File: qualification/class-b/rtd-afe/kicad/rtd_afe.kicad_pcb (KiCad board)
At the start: 4 copper layers, 72 x 56 mm, 54 parts, among them J1 TYPE-C-31-M-12, J2 PT100, J3 SWD, U1 ADS124S08IRHBR, U2 RP2350A, U3 REF5025AIDR, U4 W25Q128JVSIQ, U5 LDO, Y1 12MHz

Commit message: SYN-363 - compact the RTD board and add angled and schematic views
Signed-off-by: nyagamunene <stevenyaga2014@gmail.com>
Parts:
- moved H4 7.21 mm to (64.0, 49.0)
- moved J1 6.25 mm to (55.0, 5.24)
- moved C_L1 6.00 mm to (58.5, 20.0)
- moved C_L2 6.00 mm to (63.0, 21.5)
- moved D1 6.00 mm to (52.5, 16.0)
- moved D2 6.00 mm to (56.0, 16.0)
- moved H2 6.00 mm to (64.0, 4.00)
- moved R_CC1 6.00 mm to (59.0, 12.0)
- moved R_CC2 6.00 mm to (51.0, 12.0)
- moved U5 6.00 mm to (62.0, 17.0)
- moved C_IO1 5.01 mm to (42.0, 35.0)
- moved C_F 4.61 mm to (36.0, 48.0)
- moved J3 4.47 mm to (53.5, 48.0)
- moved H3 4.00 mm to (4.00, 49.0)
- moved J2 2.50 mm to (28.8, 50.0)
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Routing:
- net SWDIO: track 23.2 -> 13.7 mm
- net VBUS: track 27.2 -> 21.2 mm
- net ADC_RESET_N: track 25.9 -> 20.3 mm
- net AIN1: track 19.8 -> 25.1 mm
- net SWCLK: track 19.6 -> 14.9 mm
- net DGND: track 4.65 -> 0.00 mm, vias 26 -> 25
- net USB_DN_C: track 21.6 -> 17.1 mm
- net USB_DP_C: track 21.6 -> 17.1 mm
- net USB_DN: track 12.2 -> 8.85 mm, vias 2 -> 0
- net RTD_FP: track 25.2 -> 28.5 mm
- net USB_DP: track 8.28 -> 11.5 mm
- net RTD_SP: track 6.98 -> 4.48 mm
- net RTD_SN: track 6.79 -> 4.29 mm
- net +3V3: track 158.3 -> 160.5 mm
- net QSPI_SD1: track 16.7 -> 18.7 mm
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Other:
- board size 72 x 56 mm -> 66 x 53 mm

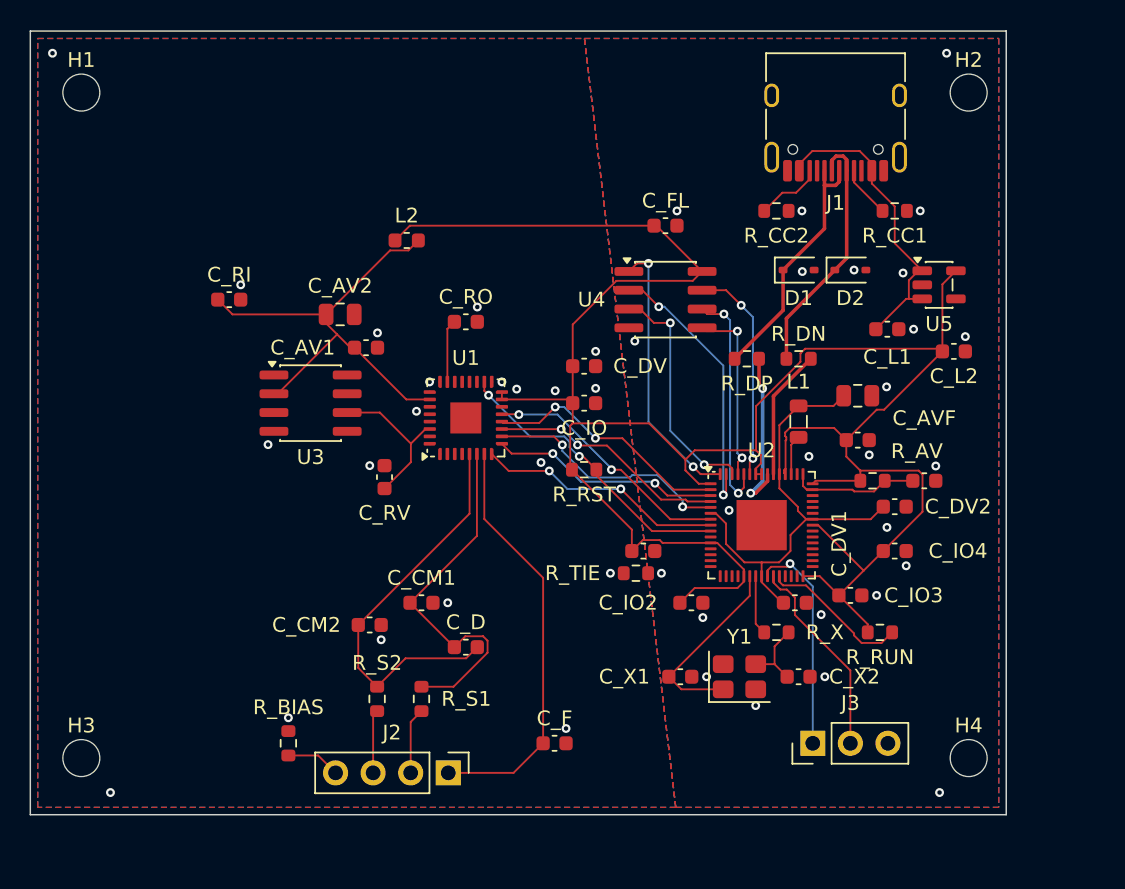
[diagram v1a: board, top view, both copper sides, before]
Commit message: SYN-363 - tighten the RTD board to 63 x 51 mm
Signed-off-by: nyagamunene <stevenyaga2014@gmail.com>
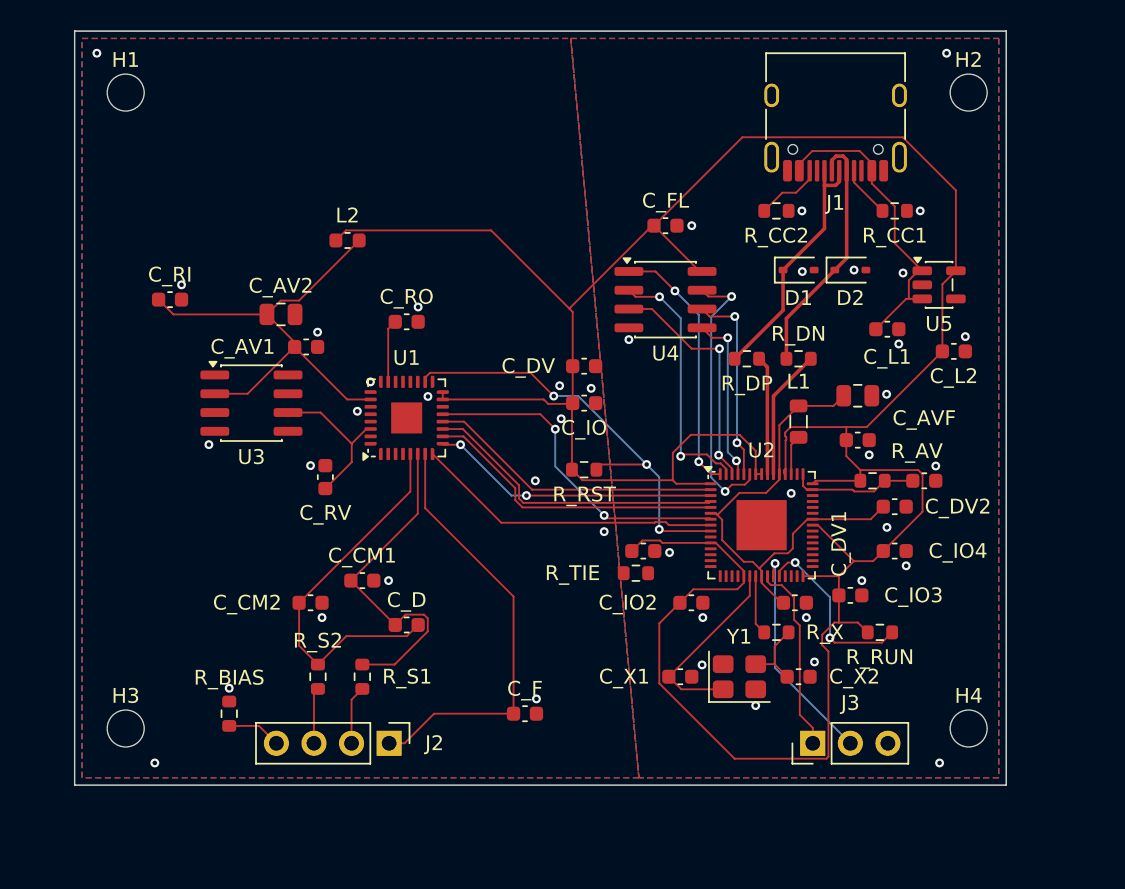
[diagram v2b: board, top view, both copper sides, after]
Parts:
- moved J2 4.47 mm to (24.8, 48.0)
- moved R_BIAS 4.47 mm to (14.0, 46.0)
- moved C_CM1 4.27 mm to (23.0, 37.0)
- moved C_CM2 4.27 mm to (19.5, 38.5)
- moved C_D 4.27 mm to (26.0, 40.0)
- moved R_S1 4.27 mm to (23.0, 43.5)
- moved R_S2 4.27 mm to (20.0, 43.5)
- moved C_AV1 4.05 mm to (19.2, 21.2)
- moved C_AV2 4.00 mm to (17.5, 19.0)
- moved C_RI 4.00 mm to (10.0, 18.0)
- moved C_RO 4.00 mm to (26.0, 19.5)
- moved C_RV 4.00 mm to (20.5, 30.0)
- moved L2 4.00 mm to (22.0, 14.0)
- moved U1 4.00 mm to (26.0, 26.0)
- moved U3 4.00 mm to (15.5, 25.0)
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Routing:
- net +3V3: track 160.5 -> 200.0 mm
- net ADC_RESET_N: track 20.3 -> 29.8 mm, vias 2 -> 3
- net ADC_DRDY: track 17.1 -> 22.5 mm
- net SPI_SCK: track 16.2 -> 20.7 mm, vias 2 -> 0
- net ADC_START: track 16.8 -> 20.8 mm, vias 2 -> 0
- net SPI_CS: track 15.6 -> 19.6 mm
- net SPI_MOSI: track 16.7 -> 20.6 mm, vias 2 -> 0
- net QSPI_SD3: track 14.9 -> 18.7 mm
- net USB_DP: track 11.5 -> 8.04 mm, vias 2 -> 0
- net SPI_MISO: track 16.9 -> 20.0 mm, vias 2 -> 0
- net RUN: track 10.1 -> 12.4 mm, vias 0 -> 2
- net QSPI_SCLK: track 15.6 -> 13.3 mm
- net SWCLK: track 14.9 -> 13.0 mm, vias 1 -> 0
- net DVDD_1V1: track 31.7 -> 33.5 mm
- net AIN1: track 25.1 -> 23.5 mm
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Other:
- board size 66 x 53 mm -> 63 x 51 mm

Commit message: SYN-363 - re-place and compact the RTD board to 50 x 44 mm
Rebuild the floorplan around the signal chain instead of scaling it: analog chain and input filter on the left, MCU/flash/crystal and USB on the right, connectors on the edges. The board drops from 63.1 x 51.1 mm to 50.1 x 44.1 mm.

- U2/U4 9.6 mm apart, Y1 below U2, USB-C at the top edge, SWD and PT100 at the bottom.
- R_TIE moved to the AGND/DGND bisector at (31.4, 31.5); all 54 ground pads sit on their own side of the split.
- 349 segments, 61 vias, 597.1 mm of copper, 41 nets connected, 0 open.
- KiCad DRC 0 errors / 0 warnings / 0 unconnected, ERC 0 errors / 2 library warnings, tie check R_TIE only.
- U1 label moved; 24 passive/TVS reference labels hidden where the compact layout has no clear spot (refdes remain in BOM, PnP, schematic).
- Record the all-absolute sidecar re-packing defect and refresh QUALIFICATION/SHA256SUMS.
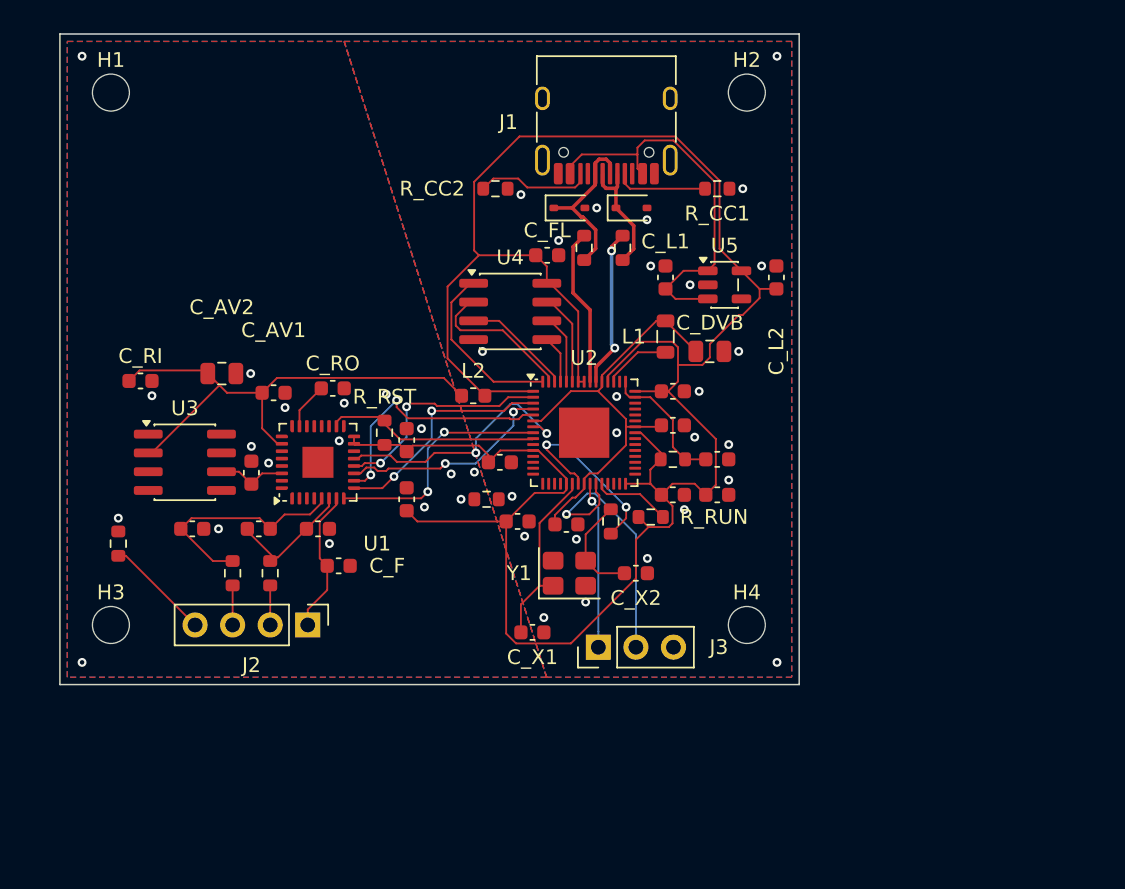
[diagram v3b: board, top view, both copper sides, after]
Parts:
- moved R_CC2 19.1 mm to (32.0, 10.5)
- moved R_RUN 17.4 mm to (42.5, 32.7)
- moved H4 16.6 mm to (49.0, 40.0)
- moved C_DV1 16.3 mm to (36.8, 33.2)
- moved C_F 16.1 mm to (21.4, 36.0)
- moved D1 16.1 mm to (37.0, 11.8)
- moved C_DV2 16.0 mm to (44.0, 26.5)
- moved J3 15.9 mm to (39.0, 41.5)
- moved J1 15.5 mm to (39.5, 5.44)
- moved C_L1 15.4 mm to (43.5, 16.5), turned to 90 degrees
- moved D2 15.4 mm to (41.2, 11.8)
- moved H2 15.0 mm to (49.0, 4.00)
- moved U5 14.5 mm to (47.5, 17.0)
- moved C_AVF 14.1 mm to (47.0, 28.8)
- moved R_DN 14.1 mm to (40.6, 14.5), turned to 90 degrees
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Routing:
- net +3V3: track 200.0 -> 159.7 mm
- net RTD_FP: track 29.3 -> 9.79 mm
- net ADC_RESET_N: track 29.8 -> 14.5 mm, vias 3 -> 0
- net AIN1: track 23.5 -> 8.72 mm
- net QSPI_SD3: track 18.7 -> 6.25 mm, vias 2 -> 0
- net AIN2: track 25.8 -> 15.6 mm
- net XOUT: track 4.04 -> 13.0 mm, vias 0 -> 2
- net QSPI_SD2: track 16.1 -> 7.40 mm, vias 2 -> 0
- net USB_DN_C: track 17.1 -> 8.45 mm
- net QSPI_SCLK: track 13.3 -> 4.80 mm, vias 2 -> 0
- net QSPI_SD0: track 11.5 -> 3.23 mm, vias 2 -> 0
- net QSPI_SD1: track 17.5 -> 10.3 mm, vias 2 -> 0
- net RUN: track 12.4 -> 5.27 mm, vias 2 -> 0
- net SPI_SCK: track 20.7 -> 14.6 mm, vias 0 -> 2
- net VREF: track 10.6 -> 4.74 mm
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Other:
- board size 63 x 51 mm -> 50 x 44 mm

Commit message: SYN-363 - level J2 with J3 at the board edge
Move J2 down 1.5 mm so both headers sit at y = 41.5 mm with their bodies 0.8 mm from the bottom edge. J2 carries no ground pads, so the AGND/DGND split and the route topology are unchanged.

Refresh the route, reports, Gerbers and renders: 339 segments, 64 vias, 586.6 mm, 41 nets, 0 open; DRC 0 errors / 0 warnings / 0 unconnected; R_TIE still the only ground tie.

Record why J1 stays at (39.5, 6.0): centering it was tried and leaves an unconnected AGND/DGND pour sliver at U2's 0.4 mm pad row that the stitching search cannot tie.
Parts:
- moved J2 1.50 mm to (19.3, 41.5)
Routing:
- net +3V3: track 159.7 -> 149.9 mm
- net XOUT: track 13.0 -> 6.86 mm
- net SWDIO: track 18.0 -> 12.4 mm
- net ADC_DRDY: track 17.4 -> 13.1 mm
- net VBUS: track 26.6 -> 29.5 mm
- net ADC_START: track 16.4 -> 18.3 mm
- net USB_DN: track 10.8 -> 12.5 mm
- net RTD_SP: track 2.67 -> 4.17 mm
- net RTD_SN: track 2.67 -> 4.17 mm
- net RTD_FP: track 9.79 -> 11.0 mm
- net RTD_FN: track 7.13 -> 8.32 mm
- net SPI_MOSI: track 17.2 -> 18.4 mm
- net QSPI_SS: track 11.9 -> 13.0 mm, vias 0 -> 2
- net SPI_MISO: track 15.4 -> 16.3 mm
- net SPI_SCK: track 14.6 -> 14.1 mm
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
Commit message: SYN-363 - notch the board and centre J1 on the top edge
Cut a 16.4 x 20 mm notch out of the empty top-left corner, leaving the main top edge x 26.4..52.59 mm so J1 at x 39.5 is centred. The left tab keeps H1 and the top-left ground fence via, and the proven route is unchanged.

J2 and J3 stay level at y = 41.5 mm, 0.8 mm from the bottom edge.

SynthSpec has no non-rectangular outline primitive, so check.sh applies cut_outline.py after export and re-exports the Gerbers/drill from the cut board. DRC 0 errors / 0 warnings / 0 unconnected; R_TIE remains the only ground tie. Board area is 1880 mm², down from the rectangular 2208 mm² and the original 3536 mm².
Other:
- board size 50 x 44 mm -> 50.1 x 44.1 mm
- net class Default removed
- net class Power removed
- net class USB removed
